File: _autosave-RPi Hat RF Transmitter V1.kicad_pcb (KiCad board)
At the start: 4 copper layers, 65 x 56 mm, 83 parts, among them CON1 Sig_In, CON2 SMA-, IC1 ADG904BRUZ-R, IC3 SN74HC139PW, IC4 ADG904BRUZ-R, J1 Conn_02x03_Odd_Even, J10 U.FL-R-SMT(10), J11 U.FL-R-SMT(10), J12 U.FL-R-SMT(10), J3 40HAT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

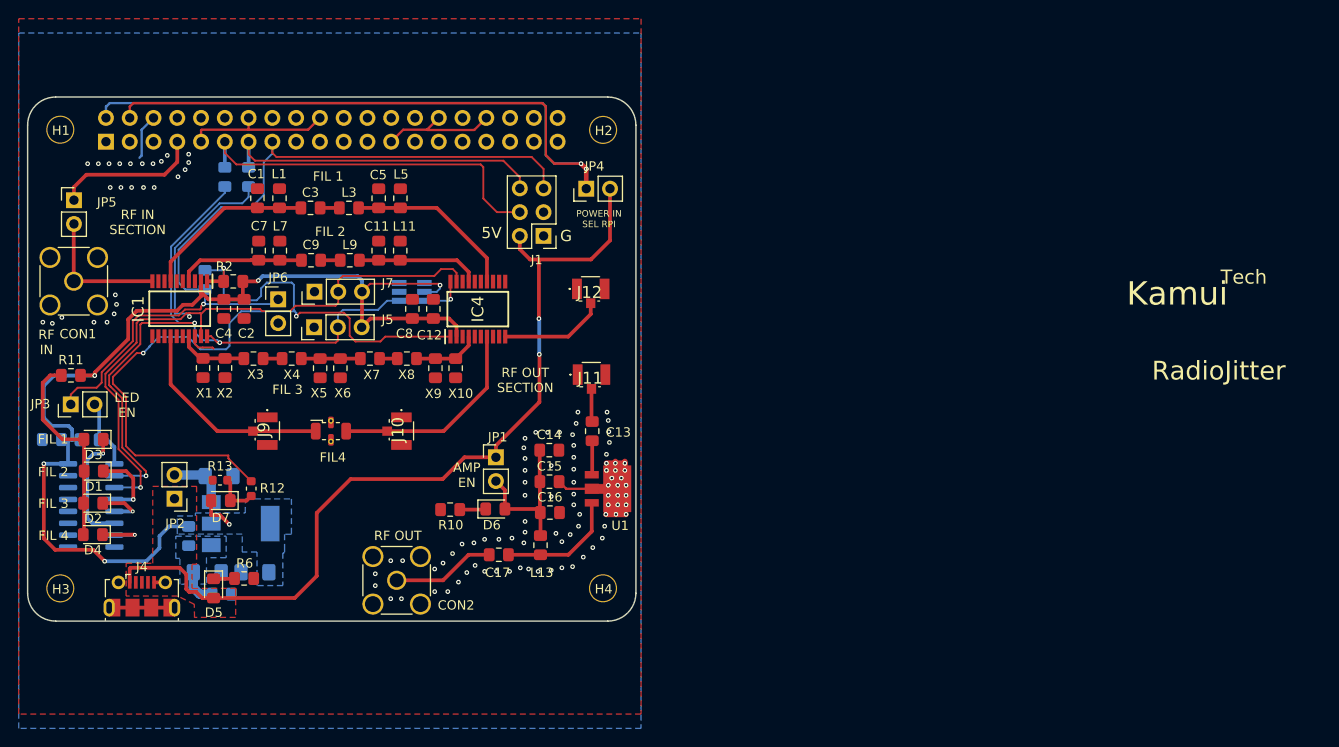
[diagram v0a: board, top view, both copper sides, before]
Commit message: routed for new circuit
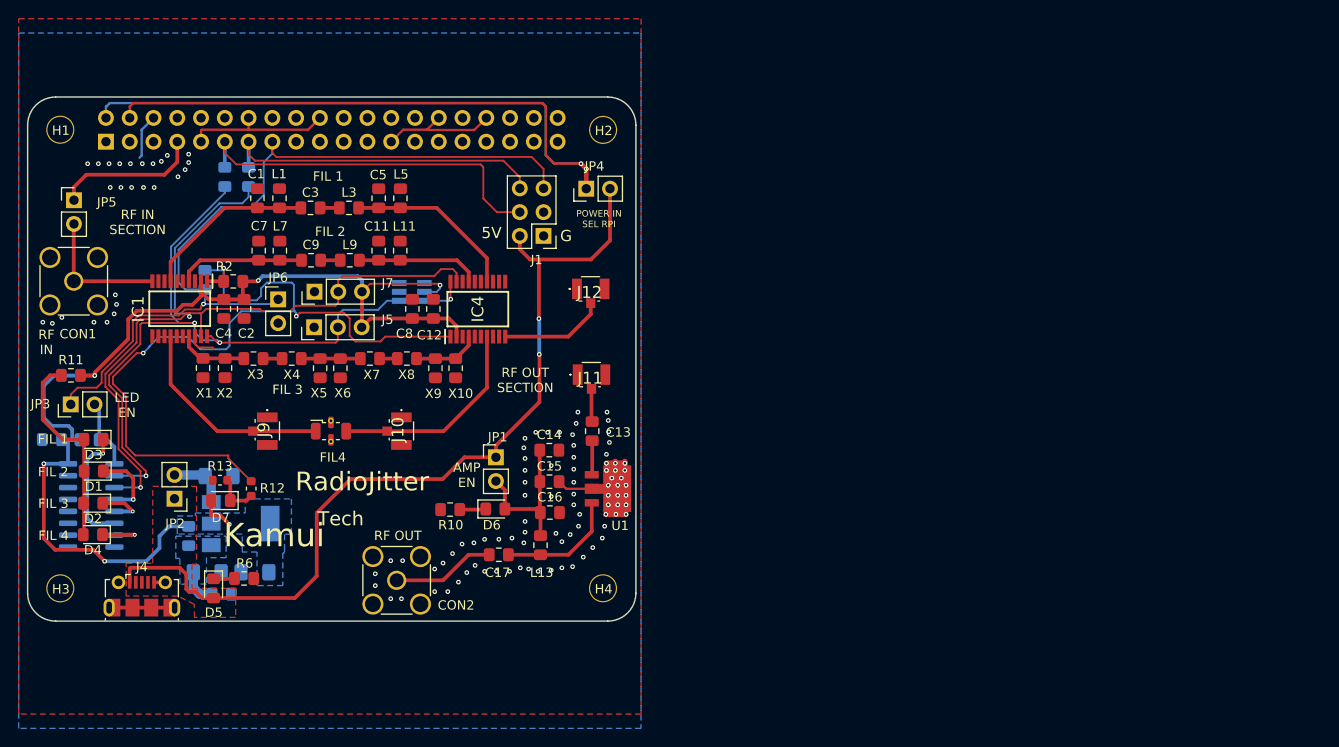
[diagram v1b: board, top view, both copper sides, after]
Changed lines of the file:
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@@
   (gr_line (start 143.546351 113.822847) (end 143.546356 63.817611) (layer Edge.Cuts) (width 0.15))
   (gr_line (start 81.546356 116.817611) (end 140.546356 116.817611) (layer Edge.Cuts) (width 0.15))
-  (gr_text RadioJitter (at 205.82 90.08) (layer F.SilkS)
+  (gr_text RadioJitter (at 114.3 101.92) (layer F.SilkS)
     (effects (font (size 2 2) (thickness 0.2)))
   )
@@
   (gr_line (start 125.984 78.105) (end 124.206 78.105) (layer B.SilkS) (width 0.15))
   (gr_line (start 125.984 84.963) (end 125.984 78.105) (layer B.SilkS) (width 0.15))
-  (gr_text Tech (at 208.502 80.062) (layer F.SilkS)
+  (gr_text Tech (at 112.002 105.882) (layer F.SilkS)
     (effects (font (size 1.5 1.5) (thickness 0.15)))
   )
-  (gr_text Kamui (at 201.39 81.84) (layer F.SilkS)
+  (gr_text Kamui (at 104.89 107.66) (layer F.SilkS)
     (effects (font (size 2.5 2.5) (thickness 0.25)))
   )
